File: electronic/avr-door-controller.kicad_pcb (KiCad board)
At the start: 2 copper layers, 110 x 56 mm, 69 parts, among them CON1 24V, J1 DOOR1, J2 DOOR2, P1 Digital, P10 DOOR2 BTN, P2 Analog, P3 DOOR1 BTN, P4 RELAY1, P5 RELAY1 CTRL, P6 USB_A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

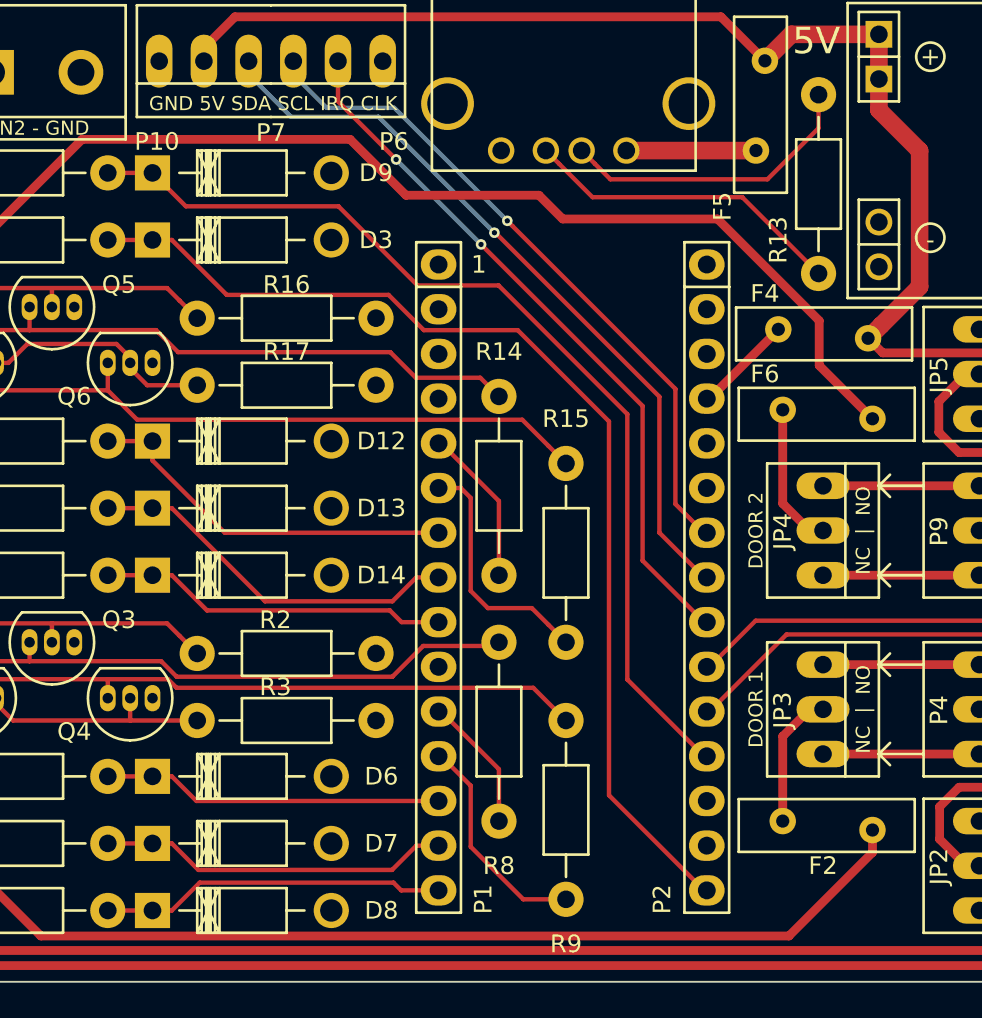
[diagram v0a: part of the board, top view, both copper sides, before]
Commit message: electronic: Add pull-down on the wiegand D0 and D1 pins
As the wiegand reader is supposed to pull-up both data lines this
should allow us to detect if the reader is not connected.

Signed-off-by: Alban Bedel <alban.bedel@avionic-design.de>
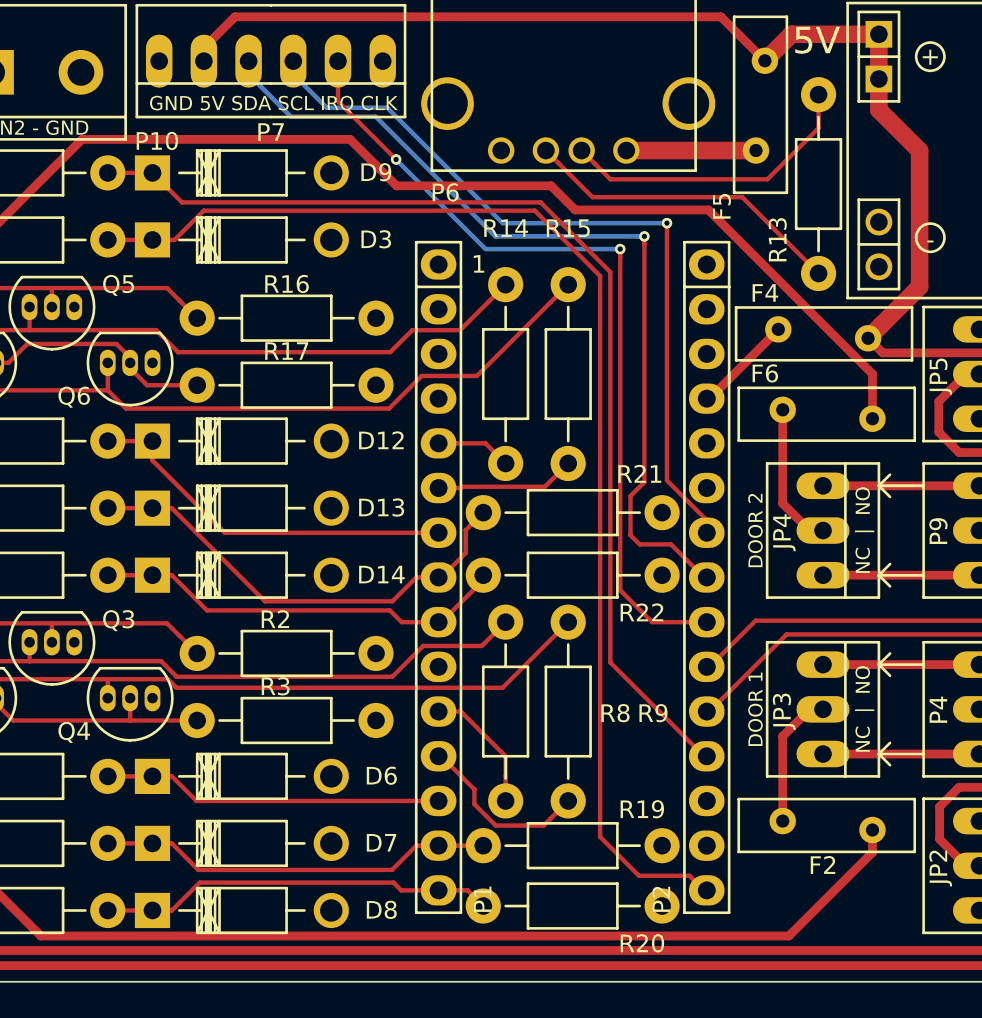
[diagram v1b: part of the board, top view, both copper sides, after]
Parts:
- added R19: 15K, Resistors_ThroughHole:Resistor_Horizontal_RM10mm, F.Cu at (142.0, 104.3)
- added R20: 15K, Resistors_ThroughHole:Resistor_Horizontal_RM10mm, F.Cu at (152.1, 107.7)
- added R21: 15K, Resistors_ThroughHole:Resistor_Horizontal_RM10mm, F.Cu at (152.1, 85.3)
- added R22: 15K, Resistors_ThroughHole:Resistor_Horizontal_RM10mm, F.Cu at (152.1, 88.9)
- moved R15 10.2 mm to (146.8, 72.4)
- moved R14 6.36 mm to (143.3, 72.4)
- moved R9 5.59 mm to (146.8, 91.6)
- moved R8 1.20 mm to (143.3, 91.6)
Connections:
- P6 pad 5: (no net) -> Net-(P6-Pad5)
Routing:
- net /D13: track 61.8 -> 69.4 mm
- net /A4: track 43.2 -> 49.7 mm
- net /D3: track 14.3 -> 7.94 mm
- net /A3: track 40.6 -> 46.9 mm
- net /A5: track 38.9 -> 44.0 mm
- net /D2: track 9.25 -> 4.28 mm
- net /D5: track 21.7 -> 26.5 mm
- net /A0: track 56.6 -> 60.8 mm
- net /D6: track 20.1 -> 23.9 mm
- net /D12: track 19.6 -> 22.5 mm
- net /D9: track 12.8 -> 10.1 mm
- net /D11: track 20.1 -> 22.7 mm
- net Net-(Q6-Pad3): track 37.9 -> 39.6 mm
- net Net-(Q5-Pad3): track 38.6 -> 39.5 mm
- net Net-(Q2-Pad2): track 36.3 -> 37.2 mm
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
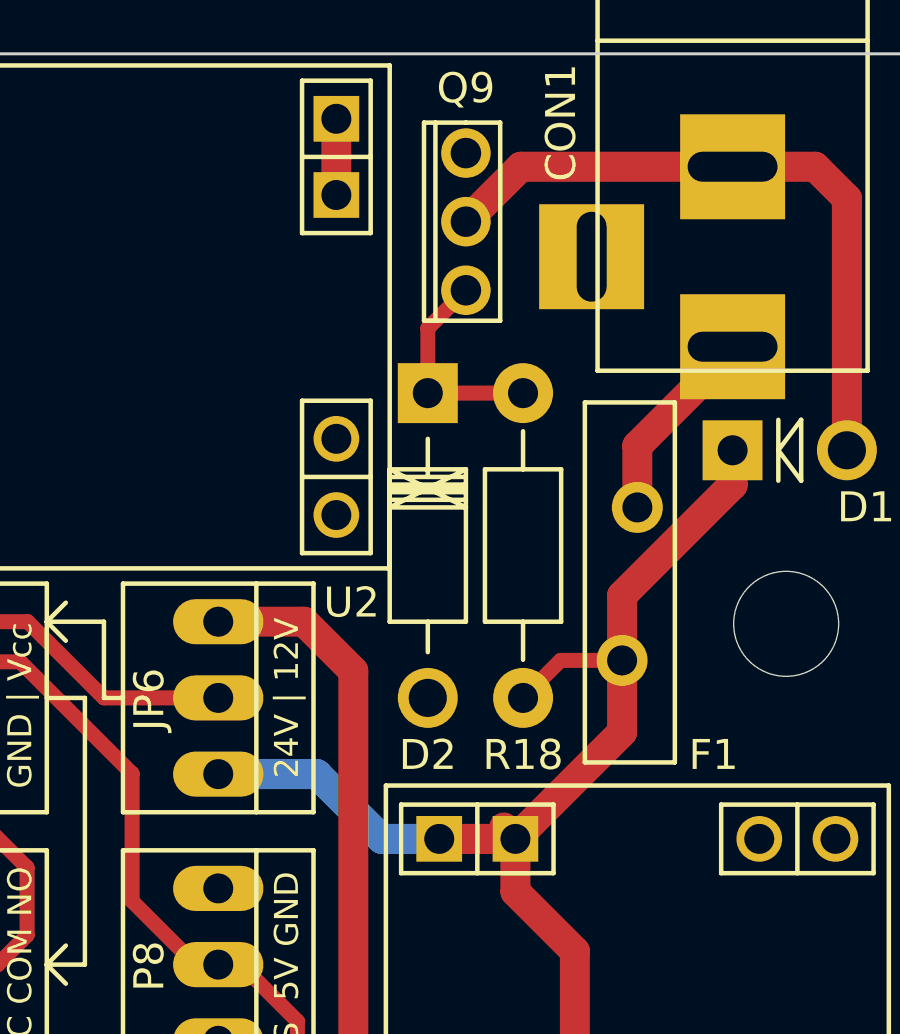
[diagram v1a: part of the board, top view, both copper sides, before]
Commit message: electronic: Fix the missing power input on the +5V regulator
Somehow the power input for the +5V regulator got removed, so the +5V
doesn't run. Add the missing supply and fix the PCB trace.

Signed-off-by: Alban Bedel <albeu@free.fr>
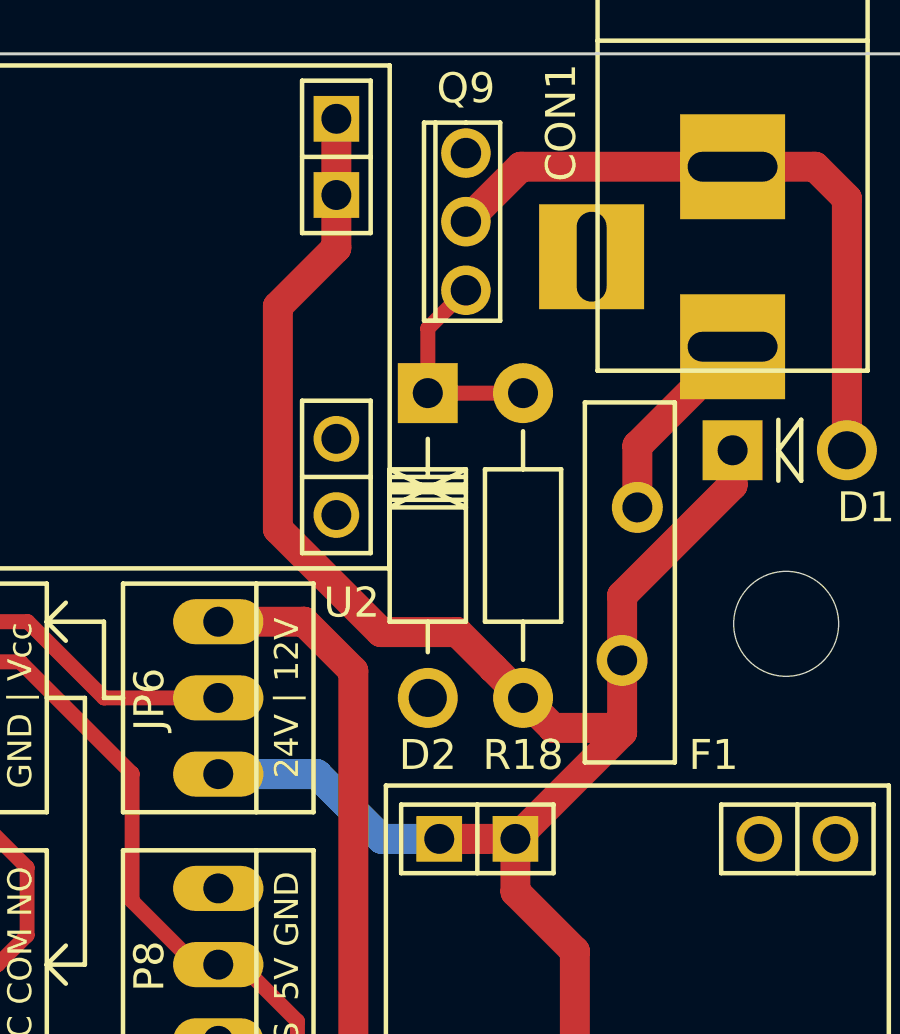
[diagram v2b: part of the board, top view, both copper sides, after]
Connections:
- U2 pad 1: Net-(U2-Pad1) -> +24V
- U2 pad 2: Net-(U2-Pad1) -> +24V
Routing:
- net +24V: track 66.9 -> 90.9 mm
- net Net-(U2-Pad1): track 2.54 -> 0.00 mm
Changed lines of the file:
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@@
 (kicad_pcb (version 4) (host pcbnew 4.0.2+dfsg1-stable)
   (general
-    (links 140)
-    (no_connects 1)
+    (links 141)
+    (no_connects 2)
     (area 91.949999 55.949999 202.050001 112.050001)
     (thickness 1.6)
     (drawings 63)
-    (tracks 392)
+    (tracks 398)
     (zones 0)
     (modules 73)
-    (nets 77)
+    (nets 76)
   )
   (page A4)
@@
   (layers
     (0 F.Cu mixed)
-    (31 B.Cu mixed)
+    (31 B.Cu mixed hide)
     (33 F.Adhes user hide)
     (35 F.Paste user hide)
@@
   )
   (setup
-    (last_trace_width 0.25)
+    (last_trace_width 1)
     (user_trace_width 0.5)
     (user_trace_width 0.75)
@@
   (net 73 "Net-(Q6-Pad2)")
   (net 74 "Net-(Q6-Pad3)")
-  (net 75 "Net-(U2-Pad1)")
-  (net 76 "Net-(P6-Pad5)")
+  (net 75 "Net-(P6-Pad5)")
   (net_class Default "This is the default net class."
     (clearance 0.2)
@@
     (add_net "Net-(Q6-Pad2)")
     (add_net "Net-(Q6-Pad3)")
-    (add_net "Net-(U2-Pad1)")
   )
   (module Mounting_Holes:MountingHole_3-5mm (layer F.Cu)
@@
     (fp_line (start -11.049 8.382) (end -11.049 -8.382) (layer F.SilkS) (width 0.15))
     (pad 2 thru_hole rect (at -9.271 4.064 180) (size 1.524 1.524) (drill 0.99822) (layers *.Cu *.Mask F.SilkS)
-      (net 75 "Net-(U2-Pad1)"))
+      (net 15 +24V))
     (pad 1 thru_hole rect (at -9.271 6.604 180) (size 1.524 1.524) (drill 0.99822) (layers *.Cu *.Mask F.SilkS)
-      (net 75 "Net-(U2-Pad1)"))
+      (net 15 +24V))
     (pad 4 thru_hole circle (at -9.271 -6.604 180) (size 1.524 1.524) (drill 0.99822) (layers *.Cu *.Mask F.SilkS)
       (net 1 GND))
@@
       (net 31 "Net-(F5-Pad2)"))
     (pad 5 thru_hole circle (at 10.16086 2.66488 90) (size 2.99974 2.99974) (drill 2.30124) (layers *.Cu *.Mask F.SilkS)
-      (net 76 "Net-(P6-Pad5)"))
+      (net 75 "Net-(P6-Pad5)"))
     (pad 5 thru_hole circle (at -3.55514 2.66488 90) (size 2.99974 2.99974) (drill 2.30124) (layers *.Cu *.Mask F.SilkS)
-      (net 76 "Net-(P6-Pad5)"))
+      (net 75 "Net-(P6-Pad5)"))
     (model Connect.3dshapes/USB_A.wrl
       (at (xyz 0.14 0 0))
@@
   (segment (start 196.215 65.89014) (end 193.04 69.06514) (width 1) (layer F.Cu) (net 13))
   (segment (start 193.04 69.06514) (end 193.04 71.12) (width 1) (layer F.Cu) (net 13))
+  (segment (start 183.007 60.706) (end 183.007 62.468) (width 1) (layer F.Cu) (net 15))
+  (segment (start 183.007 62.468) (end 181.057627 64.417373) (width 1) (layer F.Cu) (net 15))
+  (segment (start 184.492715 75.275276) (end 187.035276 75.275276) (width 1) (layer F.Cu) (net 15))
+  (segment (start 181.057627 64.417373) (end 181.057627 71.840188) (width 1) (layer F.Cu) (net 15))
+  (segment (start 181.057627 71.840188) (end 184.492715 75.275276) (width 1) (layer F.Cu) (net 15))
+  (segment (start 187.035276 75.275276) (end 188.230511 76.470511) (width 1) (layer F.Cu) (net 15))
+  (segment (start 188.230511 76.470511) (end 189.23 77.47) (width 1) (layer F.Cu) (net 15))
+  (segment (start 189.23 77.47) (end 190.229489 78.469489) (width 1) (layer F.Cu) (net 15))
+  (segment (start 190.229489 78.469489) (end 192.388489 78.469489) (width 1) (layer F.Cu) (net 15))
+  (segment (start 192.388489 78.469489) (end 192.532 78.613) (width 1) (layer F.Cu) (net 15))
   (segment (start 192.532 76.22) (end 192.532 78.613) (width 1) (layer F.Cu) (net 15))
   (segment (start 192.532 78.613) (end 188.976 82.169) (width 1) (layer F.Cu) (net 15))
@@
   (segment (start 192.532 74.05699) (end 196.215 70.37399) (width 1) (layer F.Cu) (net 15))
   (segment (start 196.215 70.37399) (end 196.215 69.215) (width 1) (layer F.Cu) (net 15))
-  (segment (start 192.532 76.22) (end 190.48 76.22) (width 0.5) (layer F.Cu) (net 15))
-  (segment (start 190.48 76.22) (end 189.23 77.47) (width 0.5) (layer F.Cu) (net 15))
-  (segment (start 188.595 81.788) (end 188.976 82.169) (width 1) (layer F.Cu) (net 15))
-  (segment (start 186.69 81.915) (end 186.436 82.169) (width 1) (layer F.Cu) (net 15))
   (segment (start 186.436 82.169) (end 184.518431 82.169) (width 1) (layer B.Cu) (net 15))
   (segment (start 184.518431 82.169) (end 182.359431 80.01) (width 1) (layer B.Cu) (net 15))
@@
   (segment (start 183.336788 106.190702) (end 181.57749 107.95) (width 1) (layer F.Cu) (net 15))
   (segment (start 181.57749 107.95) (end 179.07 107.95) (width 1) (layer F.Cu) (net 15))
+  (segment (start 183.007 60.706) (end 183.007 58.166) (width 1) (layer F.Cu) (net 15))
   (segment (start 139.446 96.647) (end 140.712 96.647) (width 0.25) (layer F.Cu) (net 16))
   (segment (start 140.712 96.647) (end 143.256 99.191) (width 0.25) (layer F.Cu) (net 16))
@@
   (segment (start 120.65 76.835) (end 120.65 78.394775) (width 0.25) (layer F.Cu) (net 74))
   (segment (start 120.65 76.835) (end 120.65 76.708575) (width 0.25) (layer F.Cu) (net 74))
-  (segment (start 183.007 60.706) (end 183.007 58.166) (width 1) (layer F.Cu) (net 75))
   (zone (net 1) (net_name GND) (layer B.Cu) (hatch edge 0.508)
     (connect_pads (clearance 0.508))

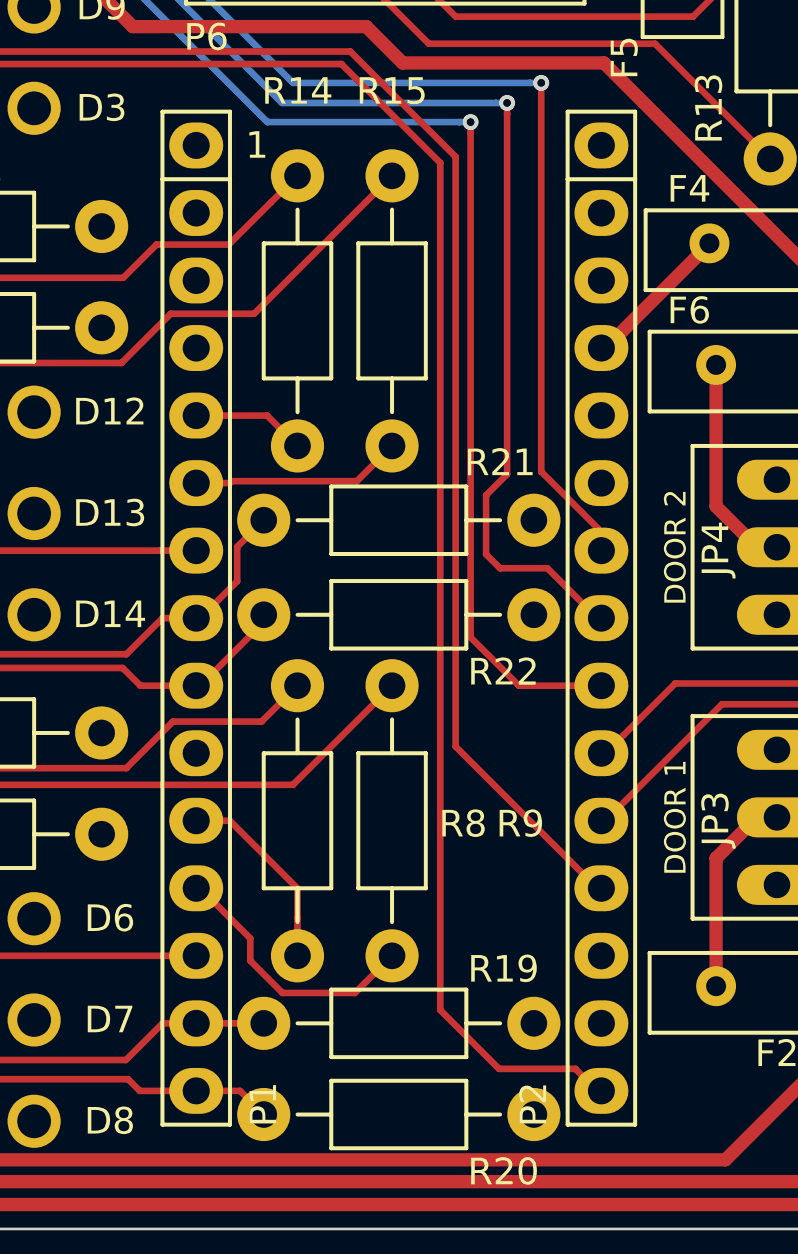
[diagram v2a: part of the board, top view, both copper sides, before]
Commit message: electronic: Move the door 1 open button to D7
Pin D13 is connected to the status LED, so that can't be used for the
door 1 open button, use D7 instead.

Signed-off-by: Alban Bedel <albeu@free.fr>
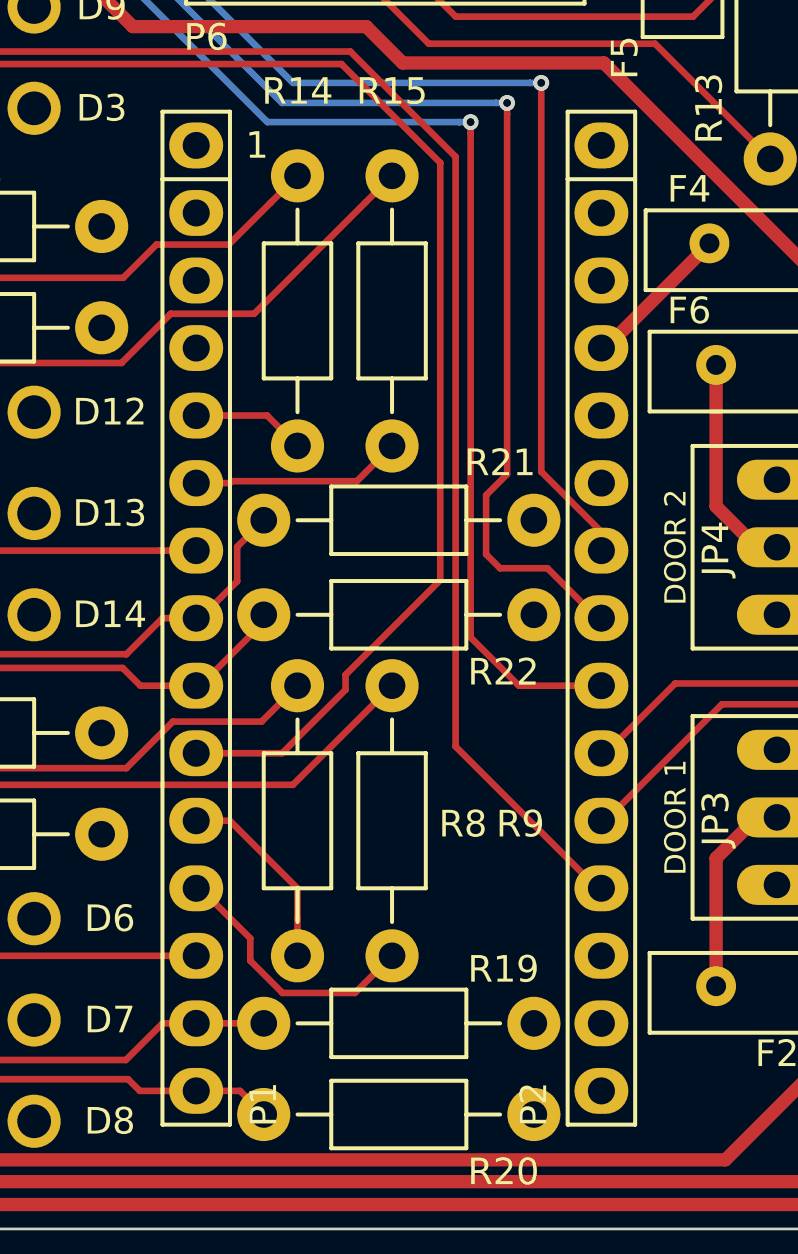
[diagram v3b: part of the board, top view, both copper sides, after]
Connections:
- D3 pad 1: /D13 -> /D7
- R1 pad 2: /D13 -> /D7
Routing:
- net /D13: track 69.4 -> 0.00 mm
- net /D7: track 0.00 -> 58.1 mm
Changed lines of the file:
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@@
     (thickness 1.6)
     (drawings 63)
-    (tracks 398)
+    (tracks 399)
     (zones 0)
     (modules 73)
@@
   )
   (setup
-    (last_trace_width 1)
+    (last_trace_width 0.25)
     (user_trace_width 0.5)
     (user_trace_width 0.75)
@@
       (net 12 "Net-(P3-Pad1)"))
     (pad 2 thru_hole circle (at 10.16 0) (size 1.99898 1.99898) (drill 1.00076) (layers *.Cu *.SilkS *.Mask)
-      (net 58 /D13))
+      (net 55 /D7))
     (model Resistors_ThroughHole.3dshapes/Resistor_Horizontal_RM10mm.wrl
       (at (xyz 0.2 0 0))
@@
       (net 1 GND))
     (pad 1 thru_hole rect (at 0 -0.00254 180) (size 1.99898 1.99898) (drill 1.00076) (layers *.Cu *.Mask F.SilkS)
-      (net 58 /D13))
+      (net 55 /D7))
     (model Diodes_ThroughHole.3dshapes/Diode_DO-35_SOD27_Horizontal_RM10.wrl
       (at (xyz 0.2 0 0))
@@
   (segment (start 172.697214 85.381383) (end 171.718597 86.36) (width 0.5) (layer F.Cu) (net 52))
   (segment (start 171.718597 86.36) (end 170.18 86.36) (width 0.5) (layer F.Cu) (net 52))
-  (segment (start 123.18948 69.85) (end 124.43897 69.85) (width 0.25) (layer F.Cu) (net 58))
-  (segment (start 124.43897 69.85) (end 126.103663 68.185307) (width 0.25) (layer F.Cu) (net 58))
-  (segment (start 126.103663 68.185307) (end 144.909307 68.185307) (width 0.25) (layer F.Cu) (net 58))
-  (segment (start 153.70534 105.97874) (end 154.5336 106.807) (width 0.25) (layer F.Cu) (net 58))
-  (segment (start 154.5336 106.807) (end 154.686 106.807) (width 0.25) (layer F.Cu) (net 58))
-  (segment (start 144.909307 68.185307) (end 148.625601 71.901601) (width 0.25) (layer F.Cu) (net 58))
-  (segment (start 148.625601 71.901601) (end 148.625601 103.768747) (width 0.25) (layer F.Cu) (net 58))
-  (segment (start 148.625601 103.768747) (end 150.835594 105.97874) (width 0.25) (layer F.Cu) (net 58))
-  (segment (start 150.835594 105.97874) (end 153.70534 105.97874) (width 0.25) (layer F.Cu) (net 58))
-  (segment (start 123.19 69.85) (end 120.65 69.85) (width 0.25) (layer F.Cu) (net 58))
+  (segment (start 123.18948 69.85) (end 124.43897 69.85) (width 0.25) (layer F.Cu) (net 55))
+  (segment (start 145.063426 91.719822) (end 142.676248 94.107) (width 0.25) (layer F.Cu) (net 55))
+  (segment (start 142.676248 94.107) (end 140.712 94.107) (width 0.25) (layer F.Cu) (net 55))
+  (segment (start 124.43897 69.85) (end 126.103663 68.185307) (width 0.25) (layer F.Cu) (net 55))
+  (segment (start 126.103663 68.185307) (end 144.909307 68.185307) (width 0.25) (layer F.Cu) (net 55))
+  (segment (start 144.909307 68.185307) (end 148.625601 71.901601) (width 0.25) (layer F.Cu) (net 55))
+  (segment (start 148.625601 71.901601) (end 148.625601 87.594399) (width 0.25) (layer F.Cu) (net 55))
+  (segment (start 148.625601 87.594399) (end 145.063426 91.156574) (width 0.25) (layer F.Cu) (net 55))
+  (segment (start 145.063426 91.156574) (end 145.063426 91.719822) (width 0.25) (layer F.Cu) (net 55))
+  (segment (start 140.712 94.107) (end 139.446 94.107) (width 0.25) (layer F.Cu) (net 55))
+  (segment (start 123.19 69.85) (end 120.65 69.85) (width 0.25) (layer F.Cu) (net 55))
   (segment (start 114.046 60.325) (end 114.046 62.484) (width 0.25) (layer F.Cu) (net 59))
   (segment (start 114.046 62.484) (end 110.49 66.04) (width 0.25) (layer F.Cu) (net 59))
